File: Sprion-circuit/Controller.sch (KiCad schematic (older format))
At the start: 1 part, among them U3 STM32F405RGTx

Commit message: z
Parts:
- added C? (x2): 2.2u, symbol Device:C
- added D?: SK6812MINI, LED_SMD:LED_SK6812MINI_PLCC4_3.5x3.5mm_P1.75mm, symbol LED:SK6812MINI
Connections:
- net +3V3: now reaches U3.1 (VBAT)
- net +3V3: now also U3.19 (VDD), U3.32 (VDD), U3.48 (VDD), U3.64 (VDD)
- net MD2_CS: now reaches U3.10 (PC2)
- net GND: now reaches U3.12 (VSSA)
- net GND: now also U3.18 (VSS), U3.60 (BOOT0), U3.63 (VSS), C?.2, C?.2
- net +3.3VA: now reaches U3.13 (VDDA)
- net IRLED_FRONT: now reaches U3.14 (PA0)
- net IRLED_SIDE: now reaches U3.15 (PA1)
- net SENSOR_WALL_FR: now reaches U3.24 (PC4)
- net SENSOR_WALL_FL: now reaches U3.25 (PC5)
- net SENSOR_WALL_SL: now reaches U3.26 (PB0)
- net SENSOR_WALL_SR: now reaches U3.27 (PB1)
- net at U3.31 (VCAP_1): now also C?.1
- net SPEAKER: now reaches U3.35 (PB14)
- net ENCODER_1A: now reaches U3.37 (PC6)
- net ENCODER_1A: now also U3.58 (PB6)
- net ENCODER_1B: now reaches U3.38 (PC7)
- net ENCODER_1B: now also U3.59 (PB7)
- net MD1_IN1: now reaches U3.41 (PA8)
- net MD1_IN2: now reaches U3.42 (PA9)
- net MD2_IN1: now reaches U3.43 (PA10)
- net MD2_IN2: now reaches U3.44 (PA11)
- net at U3.47 (VCAP_2): now also C?.1
- net IMU_SCK: now reaches U3.55 (PB3)
- net IMU_MISO: now reaches U3.56 (PB4)
- net IMU_MOSI: now reaches U3.57 (PB5)
- net IMU_CS: now reaches U3.61 (PB8)
- net FULLCOLOR_LED: now reaches U3.62 (PB9)
- net RESET: now reaches U3.7 (NRST)
- net BATT: now reaches U3.8 (PC0)
- net MD1_CS: now reaches U3.9 (PC1)
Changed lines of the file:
@@
 $Descr A4 11693 8268
 encoding utf-8
-Sheet 3 5
+Sheet 5 5
 Title ""
 Date ""
@@
 	1    0    0    -1
 $EndComp
+Wire Wire Line
+	3200 5300 3300 5300
+Connection ~ 3300 5300
+Wire Wire Line
+	3300 5300 3400 5300
+$Comp
+L power:GND #PWR?
+U 1 1 60EE0122
+P 3200 5300
+F 0 "#PWR?" H 3200 5050 50  0001 C CNN
+F 1 "GND" H 3205 5127 50  0000 C CNN
+F 2 "" H 3200 5300 50  0001 C CNN
+F 3 "" H 3200 5300 50  0001 C CNN
+	1    3200 5300
+	1    0    0    -1
+$EndComp
+Connection ~ 3200 5300
+$Comp
+L power:+3.3V #PWR?
+U 1 1 60EE1AE2
+P 3100 1700
+F 0 "#PWR?" H 3100 1550 50  0001 C CNN
+F 1 "+3.3V" H 3115 1873 50  0000 C CNN
+F 2 "" H 3100 1700 50  0001 C CNN
+F 3 "" H 3100 1700 50  0001 C CNN
+	1    3100 1700
+	1    0    0    -1
+$EndComp
+Wire Wire Line
+	3100 1700 3200 1700
+Connection ~ 3100 1700
+Connection ~ 3200 1700
+Wire Wire Line
+	3200 1700 3300 1700
+Connection ~ 3300 1700
+Wire Wire Line
+	3300 1700 3400 1700
+Connection ~ 3400 1700
+Wire Wire Line
+	3400 1700 3500 1700
+$Comp
+L power:+3.3VA #PWR?
+U 1 1 60EE2B83
+P 3600 1700
+F 0 "#PWR?" H 3600 1550 50  0001 C CNN
+F 1 "+3.3VA" H 3615 1873 50  0000 C CNN
+F 2 "" H 3600 1700 50  0001 C CNN
+F 3 "" H 3600 1700 50  0001 C CNN
+	1    3600 1700
+	1    0    0    -1
+$EndComp
+Text Label 2600 1900 2    50   ~ 0
+RESET
+$Comp
+L power:GND #PWR?
+U 1 1 60EE357E
+P 2450 2100
+F 0 "#PWR?" H 2450 1850 50  0001 C CNN
+F 1 "GND" V 2455 1972 50  0000 R CNN
+F 2 "" H 2450 2100 50  0001 C CNN
+F 3 "" H 2450 2100 50  0001 C CNN
+	1    2450 2100
+	0    1    1    0
+$EndComp
+Wire Wire Line
+	2450 2100 2600 2100
+Text HLabel 4250 3900 2    50   Output ~ 0
+IMU_SCK
+Text HLabel 4250 4000 2    50   Input ~ 0
+IMU_MISO
+Text HLabel 4250 4100 2    50   Output ~ 0
+IMU_MOSI
+Wire Wire Line
+	4250 3900 4000 3900
+Wire Wire Line
+	4250 4000 4000 4000
+Wire Wire Line
+	4250 4100 4000 4100
+Text HLabel 2350 4300 0    50   Input ~ 0
+ENCODER_1B
+Text HLabel 2350 4200 0    50   Input ~ 0
+ENCODER_1A
+Text HLabel 4250 4400 2    50   Output ~ 0
+IMU_CS
+Wire Wire Line
+	4250 4400 4000 4400
+Wire Wire Line
+	2350 4300 2600 4300
+Wire Wire Line
+	2350 4200 2600 4200
+Text HLabel 4250 4200 2    50   Input ~ 0
+ENCODER_1A
+Text HLabel 4250 4300 2    50   Input ~ 0
+ENCODER_1B
+Wire Wire Line
+	4250 4200 4000 4200
+Wire Wire Line
+	4250 4300 4000 4300
+Text HLabel 2350 3600 0    50   Input ~ 0
+BATT
+Wire Wire Line
+	2600 3600 2350 3600
+Text HLabel 4250 1900 2    50   Output ~ 0
+IRLED_FRONT
+Text HLabel 4250 2000 2    50   Output ~ 0
+IRLED_SIDE
+Wire Wire Line
+	4000 1900 4250 1900
+Wire Wire Line
+	4000 2000 4250 2000
+Text HLabel 4300 2700 2    50   Output ~ 0
+MD1_IN1
+Text HLabel 4300 2800 2    50   Output ~ 0
+MD1_IN2
+Text HLabel 4300 2900 2    50   Output ~ 0
+MD2_IN1
+Text HLabel 4300 3000 2    50   Output ~ 0
+MD2_IN2
+Wire Wire Line
+	4000 2700 4300 2700
+Wire Wire Line
+	4000 2800 4300 2800
+Wire Wire Line
+	4000 2900 4300 2900
+Wire Wire Line
+	4000 3000 4300 3000
+Text HLabel 2350 3700 0    50   Input ~ 0
+MD1_CS
+Text HLabel 2350 3800 0    50   Input ~ 0
+MD2_CS
+Wire Wire Line
+	2350 3700 2600 3700
+Wire Wire Line
+	2350 3800 2600 3800
+Text HLabel 2350 4000 0    50   Input ~ 0
+SENSOR_WALL_FR
+Text HLabel 2350 4100 0    50   Input ~ 0
+SENSOR_WALL_FL
+Text HLabel 4250 3700 2    50   Input ~ 0
+SENSOR_WALL_SR
+Text HLabel 4250 3600 2    50   Input ~ 0
+SENSOR_WALL_SL
+Wire Wire Line
+	4000 3600 4250 3600
+Wire Wire Line
+	4000 3700 4250 3700
+$Comp
+L Device:C C?
+U 1 1 60EF0F88
+P 1700 2300
+F 0 "C?" V 1448 2300 50  0000 C CNN
+F 1 "2.2u" V 1539 2300 50  0000 C CNN
+F 2 "" H 1738 2150 50  0001 C CNN
+F 3 "~" H 1700 2300 50  0001 C CNN
+	1    1700 2300
+	0    1    1    0
+$EndComp
+$Comp
+L Device:C C?
+U 1 1 60EF1ACA
+P 1700 2700
+F 0 "C?" V 1448 2700 50  0000 C CNN
+F 1 "2.2u" V 1539 2700 50  0000 C CNN
+F 2 "" H 1738 2550 50  0001 C CNN
+F 3 "~" H 1700 2700 50  0001 C CNN
+	1    1700 2700
+	0    1    1    0
+$EndComp
+Wire Wire Line
+	1850 2300 2600 2300
+Wire Wire Line
+	2600 2400 1850 2400
+Wire Wire Line
+	1850 2400 1850 2700
+$Comp
+L power:GND #PWR?
+U 1 1 60EF339E
+P 1400 2800
+F 0 "#PWR?" H 1400 2550 50  0001 C CNN
+F 1 "GND" H 1405 2627 50  0000 C CNN
+F 2 "" H 1400 2800 50  0001 C CNN
+F 3 "" H 1400 2800 50  0001 C CNN
+	1    1400 2800
+	1    0    0    -1
+$EndComp
+Wire Wire Line
+	1550 2700 1400 2700
+Wire Wire Line
+	1400 2700 1400 2800
+Wire Wire Line
+	1550 2300 1400 2300
+Wire Wire Line
+	1400 2300 1400 2700
+Connection ~ 1400 2700
+$Comp
+L LED:SK6812MINI D?
+U 1 1 60EFAFD7
+P 5650 6250
+F 0 "D?" H 5994 6296 50  0000 L CNN
+F 1 "SK6812MINI" H 5994 6205 50  0000 L CNN
+F 2 "LED_SMD:LED_SK6812MINI_PLCC4_3.5x3.5mm_P1.75mm" H 5700 5950 50  0001 L TNN
+F 3 "https://cdn-shop.adafruit.com/product-files/2686/SK6812MINI_REV.01-1-2.pdf" H 5750 5875 50  0001 L TNN
+	1    5650 6250
+	1    0    0    -1
+$EndComp
+Wire Wire Line
+	2350 4000 2600 4000
+Wire Wire Line
+	2350 4100 2600 4100
+Text Label 4250 5000 0    50   ~ 0
+SPEAKER
+Text Label 4250 4500 0    50   ~ 0
+FULLCOLOR_LED
+Wire Wire Line
+	4000 4500 4250 4500
+Wire Wire Line
+	4000 5000 4250 5000
 $EndSCHEMATC

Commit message: :fix　いろいろ
後で書きます
とりあえず寝ます
許してください
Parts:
- added C30, C31, C33, C34, C35: 0.1u, symbol Device:C
- added C32: C, symbol Device:C
- added J2: Conn_01x04_Female, symbol Connector:Conn_01x04_Female
- added LS1: Speaker, symbol Device:Speaker
- added Q3, Q4: Q_NMOS_GSD, symbol Device:Q_NMOS_GSD
- added R33, R34, R35, R36, R37: R, symbol Device:R
- added SW2, SW3, SW4: SW_Push, symbol Switch:SW_Push
- gave numbers to parts that had none: 3
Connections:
- net +3.3VA: now also C35.1
- net +3V3: now also C30.1, C31.1, C33.1, C34.1, Q4.1 (G), R36.1, SW3.2, SW4.2
- net FULLCOLOR_LED: now also Q4.2 (S), R36.2
- net GND: now also D10.2 (VSS), C30.2, C31.2, C32.2, C33.2, C34.2, C35.2, J2.4 (Pin_4), Q3.2 (S), R34.2, SW2.2
- net RESET: now also C32.1, J2.1 (Pin_1), SW2.1
- net SPEAKER: now also Q3.1 (G), R34.1
- net at D10.3 (DIN): now also Q4.3 (D), R37.2
- net +5V: now reaches D10.4 (VDD)
- net +5V: now also R37.1
- net SW1: now reaches U3.33 (PB12)
- net SW1: now also SW4.1
- net SW2: now reaches U3.34 (PB13)
- net SW2: now also SW3.1
- net SWDIO: now reaches U3.46 (PA13)
- net SWDIO: now also J2.2 (Pin_2)
- net SWDCLK: now reaches U3.49 (PA14)
- net SWDCLK: now also J2.3 (Pin_3)
- new net: LS1.1, R33.1, R35.2
- new net: LS1.2, Q3.3 (D), R33.2
- new net +BATT: R35.1
- no-connect marks 0 -> 25
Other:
- moved on the sheet: C28, C29, D10, U3

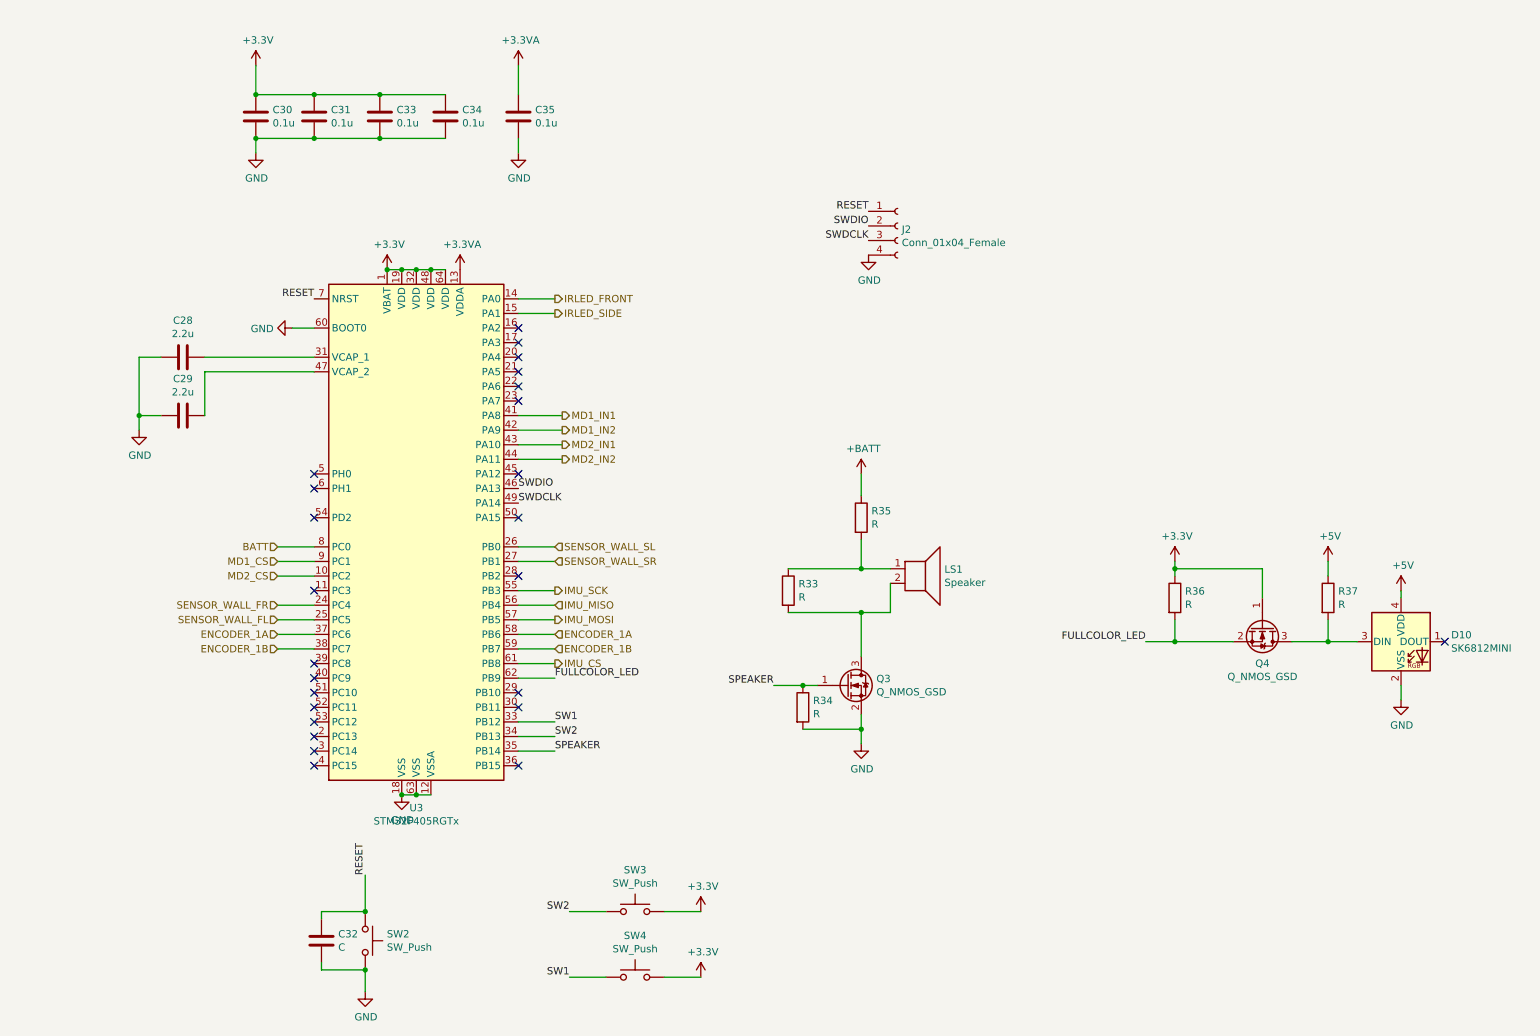
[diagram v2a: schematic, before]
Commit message: fix: MD周り,タイマー割り当て
MDの書き方を変えた
タイマー割り当てを再構成、対称性・高性能タイマーをどうするかみたいなとこ
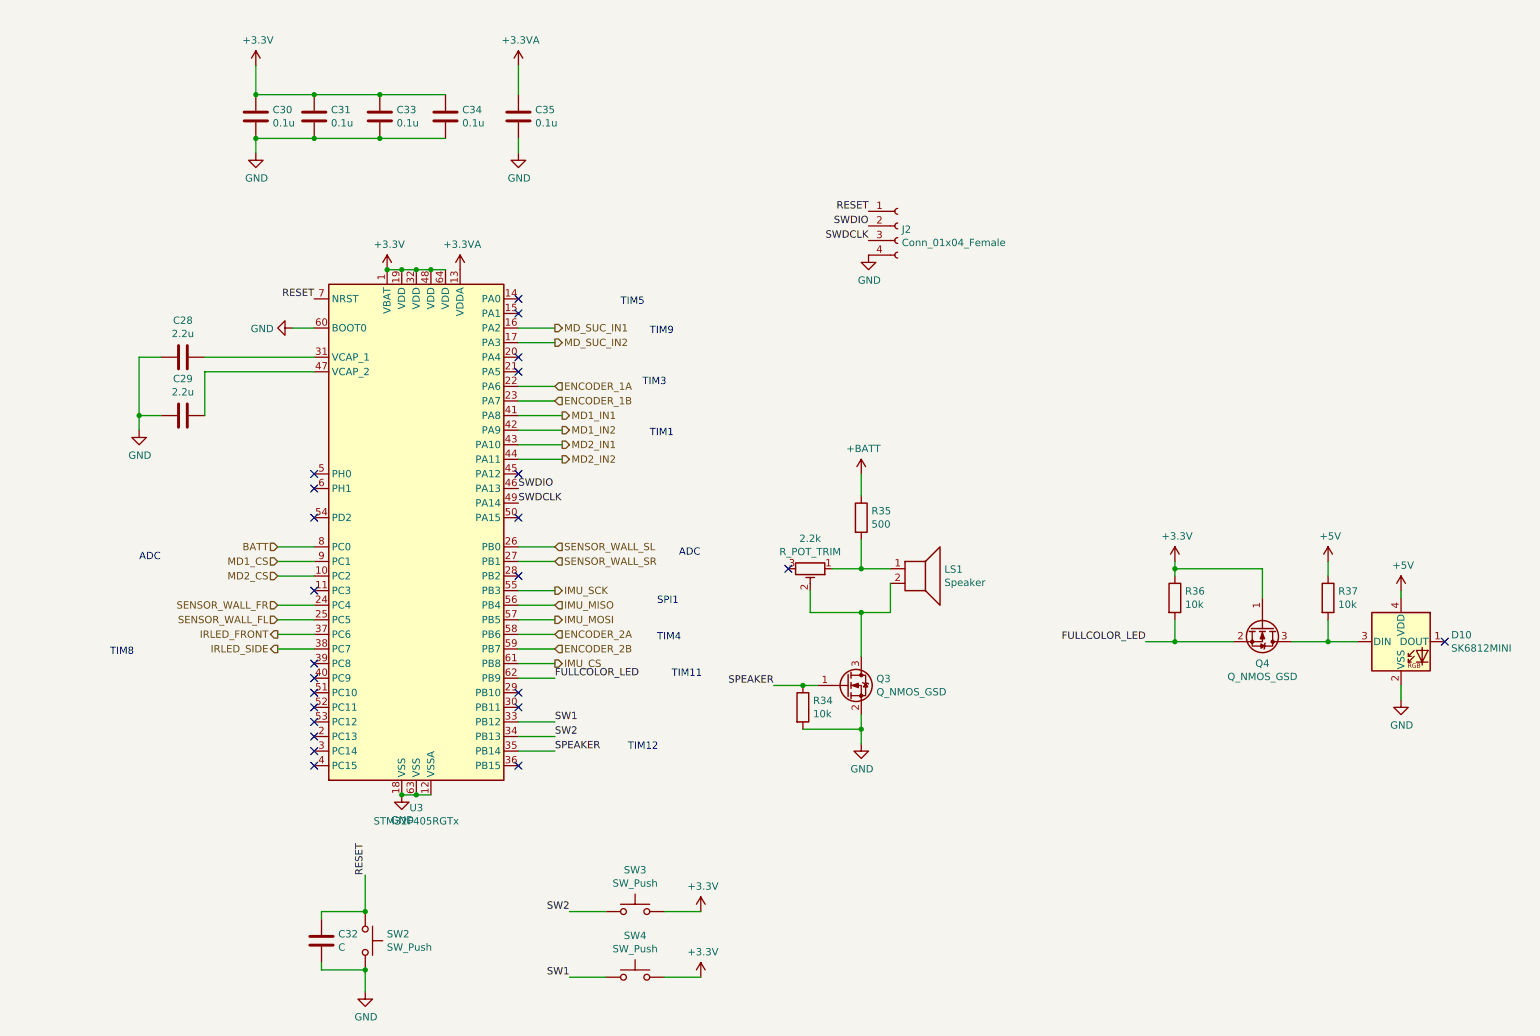
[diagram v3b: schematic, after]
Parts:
- removed R33: R, symbol Device:R
- added 2.2k: R_POT_TRIM, symbol Device:R_POT_TRIM
- R34, R36, R37: value R -> 10k
- R35: value R -> 500
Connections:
- net ENCODER_1A: now also U3.22 (PA6); no longer U3.37 (PC6), U3.58 (PB6)
- net ENCODER_1B: now also U3.23 (PA7); no longer U3.38 (PC7), U3.59 (PB7)
- net IRLED_FRONT: now also U3.37 (PC6); no longer U3.14 (PA0)
- net IRLED_SIDE: now also U3.38 (PC7); no longer U3.15 (PA1)
- net MD_SUC_IN1: now reaches U3.16 (PA2)
- net MD_SUC_IN2: now reaches U3.17 (PA3)
- net at LS1.1, R35.2: now also 2.2k.1
- net at LS1.2, Q3.3 (D): now also 2.2k.2
- new net ENCODER_2A: U3.58 (PB6)
- new net ENCODER_2B: U3.59 (PB7)
- no-connect marks 25 -> 24
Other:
- note added: "ADC\n"
- note added: "ADC\n\n"
- note added: "SPI1\n"
- note added: "TIM11\n"
- note added: "TIM12\n"
- note added: "TIM1\n"
- note added: "TIM3\n"
- note added: "TIM4\n"
- note added: "TIM5\n"
- note added: "TIM8\n"
- note added: "TIM9\n"
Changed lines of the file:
@@
 $EndDescr
-$Comp
-L MCU_ST_STM32F4:STM32F405RGTx U3
-U 1 1 60F36A6E
-P 3250 4150
-F 0 "U3" H 3250 2261 50  0000 C CNN
-F 1 "STM32F405RGTx" H 3250 2170 50  0000 C CNN
-F 2 "Package_QFP:LQFP-64_10x10mm_P0.5mm" H 2650 2450 50  0001 R CNN
-F 3 "http://www.st.com/st-web-ui/static/active/en/resource/technical/document/datasheet/DM00037051.pdf" H 3250 4150 50  0001 C CNN
-	1    3250 4150
-	1    0    0    -1
-$EndComp
-Wire Wire Line
-	3150 5950 3250 5950
-Connection ~ 3250 5950
-Wire Wire Line
-	3250 5950 3350 5950
 $Comp
 L power:GND #PWR076
@@
 	1    0    0    -1
 $EndComp
-Connection ~ 3150 5950
 $Comp
 L power:+3.3V #PWR075
@@
 	1    0    0    -1
 $EndComp
-Wire Wire Line
-	3050 2350 3150 2350
-Connection ~ 3050 2350
-Connection ~ 3150 2350
-Wire Wire Line
-	3150 2350 3250 2350
-Connection ~ 3250 2350
-Wire Wire Line
-	3250 2350 3350 2350
-Connection ~ 3350 2350
-Wire Wire Line
-	3350 2350 3450 2350
 $Comp
 L power:+3.3VA #PWR077
@@
 Wire Wire Line
 	4200 4750 3950 4750
-Text HLabel 2300 4950 0    50   Input ~ 0
-ENCODER_1B
-Text HLabel 2300 4850 0    50   Input ~ 0
-ENCODER_1A
 Text HLabel 4200 5050 2    50   Output ~ 0
 IMU_CS
 Wire Wire Line
 	4200 5050 3950 5050
-Wire Wire Line
-	2300 4950 2550 4950
-Wire Wire Line
-	2300 4850 2550 4850
 Text HLabel 4200 4850 2    50   Input ~ 0
-ENCODER_1A
+ENCODER_2A
 Text HLabel 4200 4950 2    50   Input ~ 0
-ENCODER_1B
+ENCODER_2B
 Wire Wire Line
 	4200 4850 3950 4850
@@
 Wire Wire Line
 	2550 4250 2300 4250
-Text HLabel 4200 2550 2    50   Output ~ 0
-IRLED_FRONT
-Text HLabel 4200 2650 2    50   Output ~ 0
-IRLED_SIDE
-Wire Wire Line
-	3950 2550 4200 2550
-Wire Wire Line
-	3950 2650 4200 2650
-Text HLabel 4250 3350 2    50   Output ~ 0
-MD1_IN1
-Text HLabel 4250 3450 2    50   Output ~ 0
-MD1_IN2
-Text HLabel 4250 3550 2    50   Output ~ 0
-MD2_IN1
-Text HLabel 4250 3650 2    50   Output ~ 0
-MD2_IN2
-Wire Wire Line
-	3950 3350 4250 3350
-Wire Wire Line
-	3950 3450 4250 3450
-Wire Wire Line
-	3950 3550 4250 3550
-Wire Wire Line
-	3950 3650 4250 3650
 Text HLabel 2300 4350 0    50   Input ~ 0
 MD1_CS
@@
 P 9500 4600
 F 0 "R37" H 9570 4646 50  0000 L CNN
-F 1 "R" H 9570 4555 50  0000 L CNN
+F 1 "10k" H 9570 4555 50  0000 L CNN
 F 2 "" V 9430 4600 50  0001 C CNN
 F 3 "~" H 9500 4600 50  0001 C CNN
@@
 P 8450 4600
 F 0 "R36" H 8520 4646 50  0000 L CNN
-F 1 "R" H 8520 4555 50  0000 L CNN
+F 1 "10k" H 8520 4555 50  0000 L CNN
 F 2 "" V 8380 4600 50  0001 C CNN
 F 3 "~" H 8450 4600 50  0001 C CNN
@@
 $EndComp
 $Comp
-L Device:R R35
-U 1 1 6192BE5A
-P 6300 4050
-F 0 "R35" H 6370 4096 50  0000 L CNN
-F 1 "R" H 6370 4005 50  0000 L CNN
-F 2 "" V 6230 4050 50  0001 C CNN
-F 3 "~" H 6300 4050 50  0001 C CNN
-	1    6300 4050
-	1    0    0    -1
-$EndComp
-$Comp
-L Device:R R33
-U 1 1 6192D903
-P 5800 4550
-F 0 "R33" H 5870 4596 50  0000 L CNN
-F 1 "R" H 5870 4505 50  0000 L CNN
-F 2 "" V 5730 4550 50  0001 C CNN
-F 3 "~" H 5800 4550 50  0001 C CNN
-	1    5800 4550
-	1    0    0    -1
-$EndComp
-$Comp
 L Device:Q_NMOS_GSD Q3
 U 1 1 6192E391
@@
 	6300 4400 6500 4400
 Wire Wire Line
-	6300 4400 5800 4400
-Connection ~ 6300 4400
-Wire Wire Line
-	5800 4700 6300 4700
-Wire Wire Line
 	6500 4700 6500 4500
 Wire Wire Line
 	6300 4700 6300 5000
-Connection ~ 6300 4700
 Wire Wire Line
 	6300 4700 6500 4700
@@
 Wire Wire Line
 	4950 7200 5200 7200
-NoConn ~ 3950 2750
-NoConn ~ 3950 2850
 NoConn ~ 3950 2950
 NoConn ~ 3950 3050
-NoConn ~ 3950 3150
-NoConn ~ 3950 3250
 NoConn ~ 3950 3750
 NoConn ~ 3950 4050
@@
 NoConn ~ 2550 5350
 NoConn ~ 2550 5250
-NoConn ~ 2550 5150
-NoConn ~ 2550 5050
 NoConn ~ 2550 4550
 NoConn ~ 2550 4050
@@
 P 5900 5350
 F 0 "R34" H 5970 5396 50  0000 L CNN
-F 1 "R" H 5970 5305 50  0000 L CNN
+F 1 "10k" H 5970 5305 50  0000 L CNN
 F 2 "" V 5830 5350 50  0001 C CNN
 F 3 "~" H 5900 5350 50  0001 C CNN
@@
 Wire Wire Line
 	6300 5500 6300 5600
+Wire Wire Line
+	3950 3350 4250 3350
+Wire Wire Line
+	3950 3650 4250 3650
+Wire Wire Line
+	3950 3550 4250 3550
+Wire Wire Line
+	3950 3450 4250 3450
+Text HLabel 4250 3650 2    50   Output ~ 0
+MD2_IN2
+Text HLabel 4250 3550 2    50   Output ~ 0
+MD2_IN1
+Text HLabel 4250 3450 2    50   Output ~ 0
+MD1_IN2
+Text HLabel 4250 3350 2    50   Output ~ 0
+MD1_IN1
+Text Notes 4850 3500 0    50   ~ 0
+TIM1\n
+Text Notes 4900 4900 0    50   ~ 0
+TIM4\n
+Text Notes 4900 4650 0    50   ~ 0
+SPI1\n
+Text Notes 5050 4400 0    50   ~ 0
+ADC\n\n
+Text Notes 4700 5650 0    50   ~ 0
+TIM12\n
+Text Notes 1350 4350 0    50   ~ 0
+ADC\n
+Text Notes 1150 5000 0    50   ~ 0
+TIM8\n
+Text Notes 4650 2600 0    50   ~ 0
+TIM5\n
+Text HLabel 4200 2750 2    50   Output ~ 0
+MD_SUC_IN1
+Text HLabel 4200 2850 2    50   Output ~ 0
+MD_SUC_IN2
+Wire Wire Line
+	2550 4850 2300 4850
+Wire Wire Line
+	2550 4950 2300 4950
+Text HLabel 2300 4950 0    50   Output ~ 0
+IRLED_SIDE
+Text HLabel 2300 4850 0    50   Output ~ 0
+IRLED_FRONT
+Wire Wire Line
+	3950 2850 4200 2850
+Wire Wire Line
+	4200 2750 3950 2750
+Wire Wire Line
+	3950 3150 4200 3150
+Wire Wire Line
+	3950 3250 4200 3250
+Text HLabel 4200 3250 2    50   Input ~ 0
+ENCODER_1B
+Text HLabel 4200 3150 2    50   Input ~ 0
+ENCODER_1A
+Text Notes 4800 3150 0    50   ~ 0
+TIM3\n
+Wire Wire Line
+	3250 5950 3350 5950
+Wire Wire Line
+	3150 5950 3250 5950
+Connection ~ 3250 5950
+Connection ~ 3150 5950
+Wire Wire Line
+	3350 2350 3450 2350
+Connection ~ 3350 2350
+Wire Wire Line
+	3250 2350 3350 2350
+Connection ~ 3250 2350
+Wire Wire Line
+	3150 2350 3250 2350
+Wire Wire Line
+	3050 2350 3150 2350
+Connection ~ 3150 2350
+Connection ~ 3050 2350
+$Comp
+L MCU_ST_STM32F4:STM32F405RGTx U3
+U 1 1 60F36A6E
+P 3250 4150
+F 0 "U3" H 3250 2261 50  0000 C CNN
+F 1 "STM32F405RGTx" H 3250 2170 50  0000 C CNN
+F 2 "Package_QFP:LQFP-64_10x10mm_P0.5mm" H 2650 2450 50  0001 R CNN
+F 3 "http://www.st.com/st-web-ui/static/active/en/resource/technical/document/datasheet/DM00037051.pdf" H 3250 4150 50  0001 C CNN
+	1    3250 4150
+	1    0    0    -1
+$EndComp
+Text Notes 5000 5150 0    50   ~ 0
+TIM11\n
+NoConn ~ 3950 2550
+NoConn ~ 3950 2650
+Text Notes 4850 2800 0    50   ~ 0
+TIM9\n
+NoConn ~ 2550 5050
+NoConn ~ 2550 5150
+$Comp
+L Device:R R35
+U 1 1 6192BE5A
+P 6300 4050
+F 0 "R35" H 6370 4096 50  0000 L CNN
+F 1 "500" H 6370 4005 50  0000 L CNN
+F 2 "" V 6230 4050 50  0001 C CNN
+F 3 "~" H 6300 4050 50  0001 C CNN
+	1    6300 4050
+	1    0    0    -1
+$EndComp
+$Comp
+L Device:R_POT_TRIM 2.2k
+U 1 1 61BEE8D3
+P 5950 4400
+F 0 "2.2k" V 5743 4400 50  0000 C CNN
+F 1 "R_POT_TRIM" V 5834 4400 50  0000 C CNN
+F 2 "" H 5950 4400 50  0001 C CNN
+F 3 "~" H 5950 4400 50  0001 C CNN
+	1    5950 4400
+	0    1    1    0
+$EndComp
+Wire Wire Line
+	6100 4400 6300 4400
+Connection ~ 6300 4400
+Wire Wire Line
+	5950 4550 5950 4700
+Wire Wire Line
+	5950 4700 6300 4700
+Connection ~ 6300 4700
+NoConn ~ 5800 4400
 $EndSCHEMATC
